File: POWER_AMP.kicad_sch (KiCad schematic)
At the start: 8 parts, among them U13 SE5023L-R

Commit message: skdja7rkweg
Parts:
- removed C4, C6: 1nF, Capacitor_SMD:C_0402_1005Metric, symbol Capacitors:0402_nF1_50V
- removed C7, C8, C9: 100pF, Capacitor_SMD:C_0402_1005Metric, symbol Capacitors:0402_pF_100_50V
- added C285: 10nF, Capacitor_SMD:C_0402_1005Metric, symbol Capacitors:0402_nF010_50V
- added C4: 100nF, Capacitor_SMD:C_0603_1608Metric, symbol Capacitors:0603_nf100
- added C51: 1uF, Capacitor_SMD:C_0603_1608Metric, symbol Capacitors:0603_uF001_50V
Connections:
- net GND: now also C285.2, C4.2, C51.2
- net power detect: now reaches U13.10 (DETECT)
- net +5V renamed VCC
- net VCC: now also C285.1, C4.1, C51.1
- no-connect marks 3 -> 2
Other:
- moved on the sheet: C5

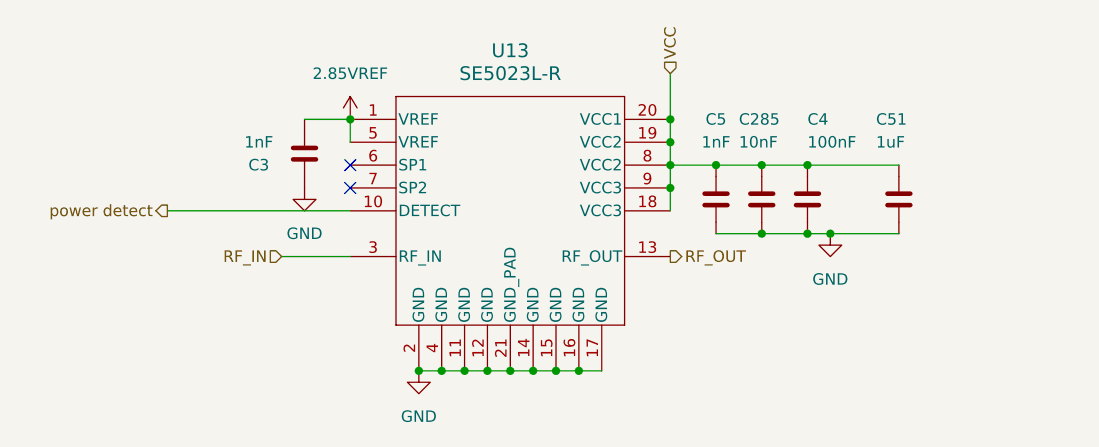
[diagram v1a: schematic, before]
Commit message: completed length matching
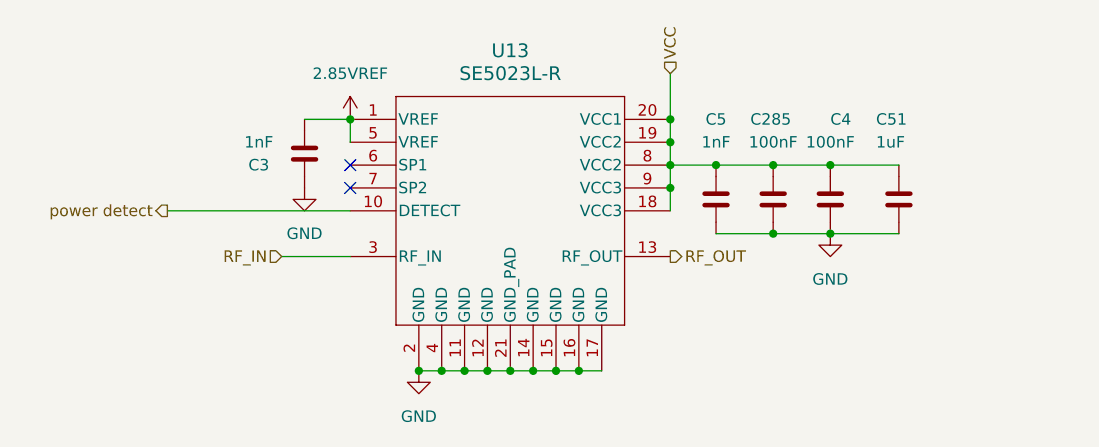
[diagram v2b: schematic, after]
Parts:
- C285: value 10nF -> 100nF; symbol Capacitors:0402_nF010_50V -> Capacitors:0402_nF100_50V; DN 490-4762-1-ND -> 490-14514-1-ND; MPN GCM155R71H103KA55D -> GCM155R71H104KE02J; price .388 -> .02
- C4: footprint Capacitor_SMD:C_0603_1608Metric -> Capacitor_SMD:C_0402_1005Metric; symbol Capacitors:0603_nf100 -> Capacitors:0402_nF100_50V; DN 490-5798-1-ND -> 490-14514-1-ND; MPN GCJ188R71H104KA12D -> GCM155R71H104KE02J; price .10 -> .02
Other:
- moved on the sheet: C285, C4
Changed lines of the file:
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@@
 	(paper "A4")
 	(junction
-		(at 96.52 99.06)
+		(at 97.79 99.06)
 		(diameter 0)
 		(color 0 0 0 0)
@@
 	)
 	(junction
+		(at 104.14 91.44)
+		(diameter 0)
+		(color 0 0 0 0)
+	)
+	(junction
 		(at 71.12 114.3)
 		(diameter 0)
@@
 	)
 	(junction
-		(at 96.52 91.44)
-		(diameter 0)
-		(color 0 0 0 0)
-	)
-	(junction
-		(at 101.6 99.06)
+		(at 97.79 91.44)
 		(diameter 0)
 		(color 0 0 0 0)
@@
 		(color 0 0 0 0)
 	)
-	(junction
-		(at 101.6 91.44)
-		(diameter 0)
-		(color 0 0 0 0)
-	)
 	(no_connect
 		(at 50.8 91.44)
@@
 	(wire
 		(pts
+			(xy 104.14 91.44) (xy 111.76 91.44)
+		)
+		(stroke
+			(width 0)
+			(type default)
+		)
+	)
+	(wire
+		(pts
 			(xy 86.36 86.36) (xy 86.36 91.44)
 		)
@@
 	(wire
 		(pts
-			(xy 91.44 91.44) (xy 96.52 91.44)
+			(xy 91.44 91.44) (xy 97.79 91.44)
 		)
 		(stroke
@@
 	(wire
 		(pts
-			(xy 91.44 99.06) (xy 96.52 99.06)
+			(xy 91.44 99.06) (xy 97.79 99.06)
+		)
+		(stroke
+			(width 0)
+			(type default)
+		)
+	)
+	(wire
+		(pts
+			(xy 97.79 91.44) (xy 104.14 91.44)
 		)
 		(stroke
@@
 	(wire
 		(pts
-			(xy 101.6 91.44) (xy 111.76 91.44)
-		)
-		(stroke
-			(width 0)
-			(type default)
-		)
-	)
-	(wire
-		(pts
-			(xy 101.6 99.06) (xy 104.14 99.06)
-		)
-		(stroke
-			(width 0)
-			(type default)
-		)
-	)
-	(wire
-		(pts
 			(xy 76.2 114.3) (xy 78.74 114.3)
 		)
@@
 	(wire
 		(pts
-			(xy 96.52 99.06) (xy 101.6 99.06)
-		)
-		(stroke
-			(width 0)
-			(type default)
-		)
-	)
-	(wire
-		(pts
-			(xy 96.52 91.44) (xy 101.6 91.44)
+			(xy 97.79 99.06) (xy 104.14 99.06)
 		)
 		(stroke
@@
 	)
 	(symbol
-		(lib_id "Capacitors:0402_nF010_50V")
-		(at 96.52 91.44 0)
+		(lib_id "Capacitors:0402_nF100_50V")
+		(at 97.79 91.44 0)
 		(unit 1)
 		(body_style 1)
@@
 		(dnp no)
 		(property "Reference" "C285"
-			(at 93.98 86.36 0)
+			(at 95.25 86.36 0)
 			(show_name no)
 			(do_not_autoplace no)
@@
 			)
 		)
-		(property "Value" "10nF"
-			(at 93.98 88.9 0)
-			(show_name no)
-			(do_not_autoplace no)
-			(effects
-				(font
-					(size 1.27 1.27)
-				)
-				(justify left)
+		(property "Value" "100nF"
+			(at 97.79 88.9 0)
+			(show_name no)
+			(do_not_autoplace no)
+			(effects
+				(font
+					(size 1.27 1.27)
+				)
 			)
 		)
 		(property "Footprint" "Capacitor_SMD:C_0402_1005Metric"
-			(at 94.742 91.44 90)
+			(at 96.012 91.44 90)
 			(hide yes)
 			(show_name no)
@@
 		)
 		(property "Datasheet" "https://ds.murata.com/simsurfing/mlcc.html?lcid=en-us&jis=false&md5=ffdf2ea84f2d70fe82acfb70297713ec"
-			(at 90.17 88.265 0)
-			(hide yes)
-			(show_name no)
-			(do_not_autoplace no)
-			(effects
-				(font
-					(size 1.27 1.27)
-				)
-			)
-		)
-		(property "Description" "10000 pF ±10% 50V Ceramic Capacitor X7R 0402 (1005 Metric)"
-			(at 91.44 83.82 0)
-			(hide yes)
-			(show_name no)
-			(do_not_autoplace no)
-			(effects
-				(font
-					(size 1.27 1.27)
-				)
-			)
-		)
-		(property "MPN" "GCM155R71H103KA55D"
-			(at 96.52 91.44 0)
-			(hide yes)
-			(show_name no)
-			(do_not_autoplace no)
-			(effects
-				(font
-					(size 1.27 1.27)
-				)
-			)
-		)
-		(property "DN" "490-4762-1-ND"
-			(at 96.52 91.44 0)
+			(at 91.44 88.265 0)
+			(hide yes)
+			(show_name no)
+			(do_not_autoplace no)
+			(effects
+				(font
+					(size 1.27 1.27)
+				)
+			)
+		)
+		(property "Description" "0.1 µF ±10% 50V Ceramic Capacitor X7R 0402 (1005 Metric)"
+			(at 92.71 83.82 0)
+			(hide yes)
+			(show_name no)
+			(do_not_autoplace no)
+			(effects
+				(font
+					(size 1.27 1.27)
+				)
+			)
+		)
+		(property "MPN" "GCM155R71H104KE02J"
+			(at 97.79 91.44 0)
+			(hide yes)
+			(show_name no)
+			(do_not_autoplace no)
+			(effects
+				(font
+					(size 1.27 1.27)
+				)
+			)
+		)
+		(property "DN" "490-14514-1-ND"
+			(at 97.79 91.44 0)
 			(hide yes)
 			(show_name no)
@@
 		)
 		(property "MFR" "Murata Electronics"
-			(at 96.52 91.44 0)
+			(at 97.79 91.44 0)
 			(hide yes)
 			(show_name no)
@@
 		)
 		(property "cost" ".02"
-			(at 96.52 91.44 0)
-			(hide yes)
-			(show_name no)
-			(do_not_autoplace no)
-			(effects
-				(font
-					(size 1.27 1.27)
-				)
-			)
-		)
-		(property "price" ".388"
-			(at 96.52 91.44 0)
+			(at 97.79 91.44 0)
+			(hide yes)
+			(show_name no)
+			(do_not_autoplace no)
+			(effects
+				(font
+					(size 1.27 1.27)
+				)
+			)
+		)
+		(property "price" ".02"
+			(at 97.79 91.44 0)
 			(hide yes)
 			(show_name no)
@@
 	)
 	(symbol
-		(lib_id "Capacitors:0603_nf100")
-		(at 101.6 91.44 0)
+		(lib_id "Capacitors:0402_nF100_50V")
+		(at 104.14 91.44 0)
 		(unit 1)
 		(body_style 1)
@@
 		(dnp no)
 		(property "Reference" "C4"
-			(at 101.6 86.36 0)
+			(at 104.14 86.36 0)
 			(show_name no)
 			(do_not_autoplace no)
@@
 		)
 		(property "Value" "100nF"
-			(at 101.6 88.9 0)
-			(show_name no)
-			(do_not_autoplace no)
-			(effects
-				(font
-					(size 1.27 1.27)
-				)
-				(justify left)
-			)
-		)
-		(property "Footprint" "Capacitor_SMD:C_0603_1608Metric"
-			(at 99.822 91.44 90)
-			(hide yes)
-			(show_name no)
-			(do_not_autoplace no)
-			(effects
-				(font
-					(size 1.27 1.27)
-				)
-			)
-		)
-		(property "Datasheet" ""
-			(at 95.25 88.265 0)
-			(hide yes)
-			(show_name no)
-			(do_not_autoplace no)
-			(effects
-				(font
-					(size 1.27 1.27)
-				)
-			)
-		)
-		(property "Description" "0.1 µF ±10% 50V Ceramic Capacitor X7R 0603 (1608 Metric)"
-			(at 96.52 83.82 0)
-			(hide yes)
-			(show_name no)
-			(do_not_autoplace no)
-			(effects
-				(font
-					(size 1.27 1.27)
-				)
-			)
-		)
-		(property "MPN" "GCJ188R71H104KA12D"
-			(at 101.6 91.44 0)
-			(hide yes)
-			(show_name no)
-			(do_not_autoplace no)
-			(effects
-				(font
-					(size 1.27 1.27)
-				)
-			)
-		)
-		(property "DN" "490-5798-1-ND"
-			(at 101.6 91.44 0)
+			(at 104.14 88.9 0)
+			(show_name no)
+			(do_not_autoplace no)
+			(effects
+				(font
+					(size 1.27 1.27)
+				)
+			)
+		)
+		(property "Footprint" "Capacitor_SMD:C_0402_1005Metric"
+			(at 102.362 91.44 90)
+			(hide yes)
+			(show_name no)
+			(do_not_autoplace no)
+			(effects
+				(font
+					(size 1.27 1.27)
+				)
+			)
+		)
+		(property "Datasheet" "https://ds.murata.com/simsurfing/mlcc.html?lcid=en-us&jis=false&md5=ffdf2ea84f2d70fe82acfb70297713ec"
+			(at 97.79 88.265 0)
+			(hide yes)
+			(show_name no)
+			(do_not_autoplace no)
+			(effects
+				(font
+					(size 1.27 1.27)
+				)
+			)
+		)
+		(property "Description" "0.1 µF ±10% 50V Ceramic Capacitor X7R 0402 (1005 Metric)"
+			(at 99.06 83.82 0)
+			(hide yes)
+			(show_name no)
+			(do_not_autoplace no)
+			(effects
+				(font
+					(size 1.27 1.27)
+				)
+			)
+		)
+		(property "MPN" "GCM155R71H104KE02J"
+			(at 104.14 91.44 0)
+			(hide yes)
+			(show_name no)
+			(do_not_autoplace no)
+			(effects
+				(font
+					(size 1.27 1.27)
+				)
+			)
+		)
+		(property "DN" "490-14514-1-ND"
+			(at 104.14 91.44 0)
 			(hide yes)
 			(show_name no)
@@
 		)
 		(property "MFR" "Murata Electronics"
-			(at 101.6 91.44 0)
-			(hide yes)
-			(show_name no)
-			(do_not_autoplace no)
-			(effects
-				(font
-					(size 1.27 1.27)
-				)
-			)
-		)
-		(property "price" ".10"
-			(at 101.6 91.44 0)
-			(hide yes)
-			(show_name no)
+			(at 104.14 91.44 0)
+			(hide yes)
+			(show_name no)
+			(do_not_autoplace no)
+			(effects
+				(font
+					(size 1.27 1.27)
+				)
+			)
+		)
+		(property "price" ".02"
+			(at 104.14 91.44 0)
+			(hide yes)
+			(show_name no)

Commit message: june_26
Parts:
- C285: cost .02 -> (none)
- C3, C5: price (none) -> .07
- U13: price (none) -> 6.3
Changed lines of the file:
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@@
+		)
+	)
+	(wire
+		(pts
+			(xy 88.9 101.6) (xy 86.36 101.6)
+		)
+		(stroke
+			(width 0)
+			(type default)
 		)
 	)
@@
 	(hierarchical_label "RF_OUT"
 		(shape output)
-		(at 86.36 101.6 0)
+		(at 88.9 101.6 0)
 		(effects
 			(font
@@
 			)
 			(justify left)
+		)
+	)
+	(netclass_flag ""
+		(length 2.54)
+		(shape round)
+		(at 44.45 101.6 180)
+		(fields_autoplaced yes)
+		(effects
+			(font
+				(size 1.27 1.27)
+			)
+			(justify right bottom)
+		)
+		(property "Net Class" "50 ohm"
+			(at 45.1485 104.14 0)
+			(show_name no)
+			(do_not_autoplace no)
+			(effects
+				(font
+					(size 1.27 1.27)
+				)
+				(justify left)
+			)
+		)
+		(property "Component Class" ""
+			(at 43.18 30.48 0)
+			(show_name no)
+			(do_not_autoplace no)
+			(effects
+				(font
+					(size 1.27 1.27)
+					(italic yes)
+				)
+			)
 		)
 	)
@@
 			)
 		)
+		(property "price" ".07"
+			(at 45.72 86.36 0)
+			(hide yes)
+			(show_name no)
+			(do_not_autoplace no)
+			(effects
+				(font
+					(size 1.27 1.27)
+				)
+			)
+		)
 		(pin "1"
 		)
@@
 		(property "DN" "490-GCM1555C1H102GA16JCT-ND"
 			(at 92.71 80.01 0)
+			(hide yes)
+			(show_name no)
+			(do_not_autoplace no)
+			(effects
+				(font
+					(size 1.27 1.27)
+				)
+			)
+		)
+		(property "price" ".07"
+			(at 91.44 91.44 0)
 			(hide yes)
 			(show_name no)
@@
 			)
 		)
-		(property "cost" ".02"
+		(property "cost" ""
 			(at 97.79 91.44 0)
 			(hide yes)
@@
 			)
 		)
+		(property "price" "6.3"
+			(at 50.8 83.82 0)
+			(hide yes)
+			(show_name no)
+			(do_not_autoplace no)
+			(effects
+				(font
+					(size 1.27 1.27)
+				)
+			)
+		)
 		(pin "13"
 		)
@@
 					(reference "U49")
 					(unit 1)
+				)
+				(path "/3d000777-5a6c-48c2-9bdf-76c34ab20cc7/9ae7c201-9480-402d-a0c4-3941bcca95cf"
+					(reference "U49")
+					(unit 1)
